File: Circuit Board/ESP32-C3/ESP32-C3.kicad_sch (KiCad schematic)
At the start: 38 parts

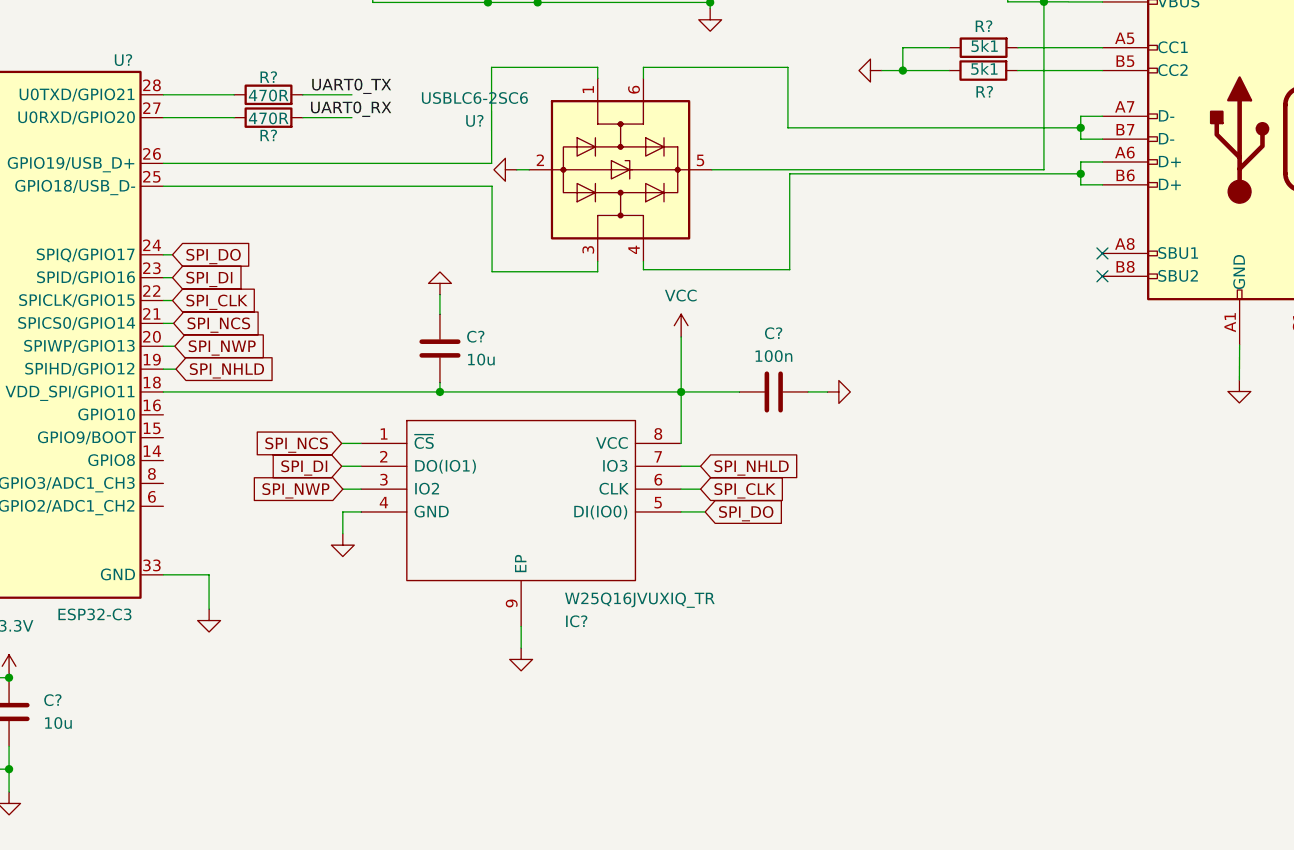
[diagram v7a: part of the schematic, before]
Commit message: Added boot loader switch
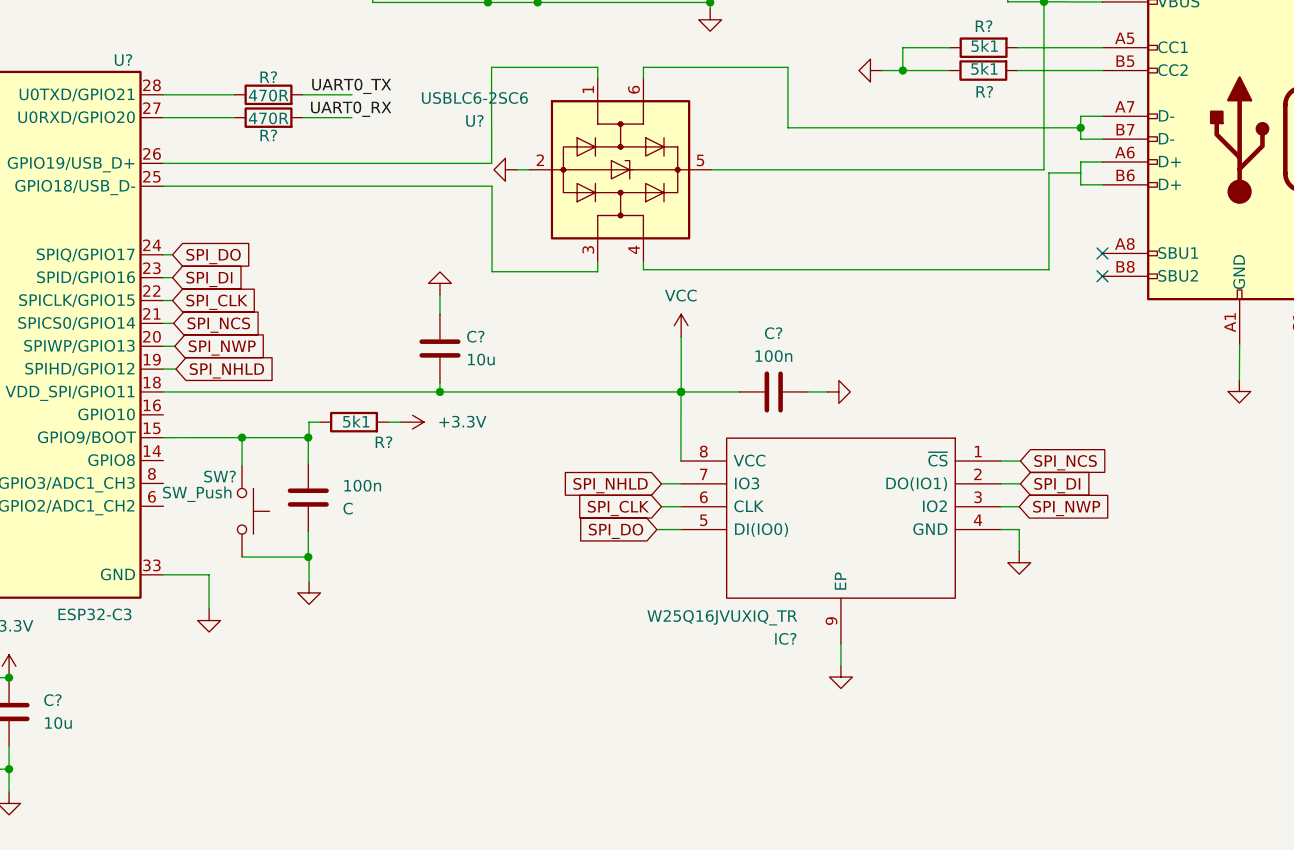
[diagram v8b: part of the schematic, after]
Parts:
- added 100n: C, symbol Device:C
- added R?: 5k1, symbol Device:R
- added SW?: SW_Push, symbol Switch:SW_Push
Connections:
- net +3.3V: now also 100n.2, R?.2, SW?.2
- net at J?.A6 (D+), J?.B6 (D+): no longer U?.4 (I/O2)
- net at U?.15 (GPIO9/BOOT): now also 100n.1, R?.1, SW?.1
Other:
- moved on the sheet: IC?
